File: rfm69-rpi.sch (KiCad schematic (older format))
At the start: 21 parts, among them IC1 RFM69, IC2 RFM69, IC3 RFM69, IC4 RFM69, IC5 NCP1117, IC6 74HC139, J1 RPi_GPIO, P1 COAX, P2 COAX, P3 COAX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

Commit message: Converted to Kicad 5 format; changed direction of INT1
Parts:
- C1, C2: symbol CP -> rfm69-rpi-rescue:CP
- IC1, IC2, IC3, IC4: symbol RFM69 -> rfm69-rpi-rescue:RFM69
- IC5: symbol LD1117S33TR -> rfm69-rpi-rescue:LD1117S33TR
- IC6: symbol 74HC139 -> rfm69-rpi-rescue:74HC139
- J1: symbol RPi_GPIO -> rfm69-rpi-rescue:RPi_GPIO
- JP1, JP2: symbol JUMPER -> rfm69-rpi-rescue:JUMPER
- P1, P2, P3, P4: symbol COAX -> rfm69-rpi-rescue:COAX
- P5: symbol CONN_01X02 -> rfm69-rpi-rescue:CONN_01X02
- R1: symbol R -> rfm69-rpi-rescue:R
- TP1, TP2: symbol TESTPAD -> rfm69-rpi-rescue:TESTPAD
- U1, U2: symbol DS18B20 -> rfm69-rpi-rescue:DS18B20

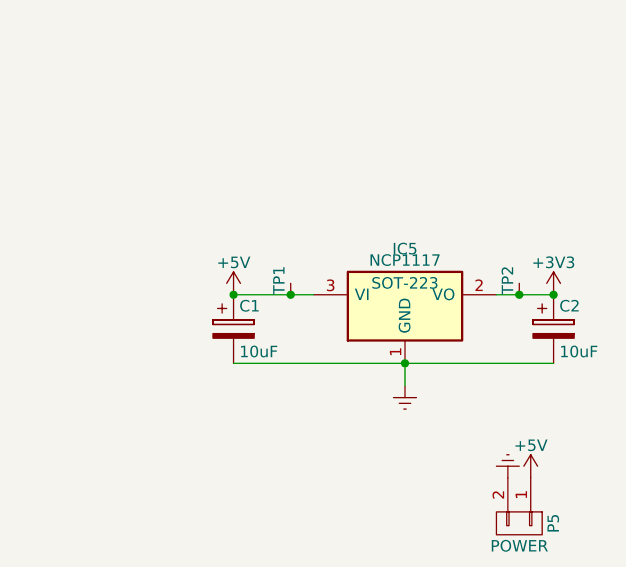
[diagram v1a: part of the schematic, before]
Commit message: Fixed RPi footprint
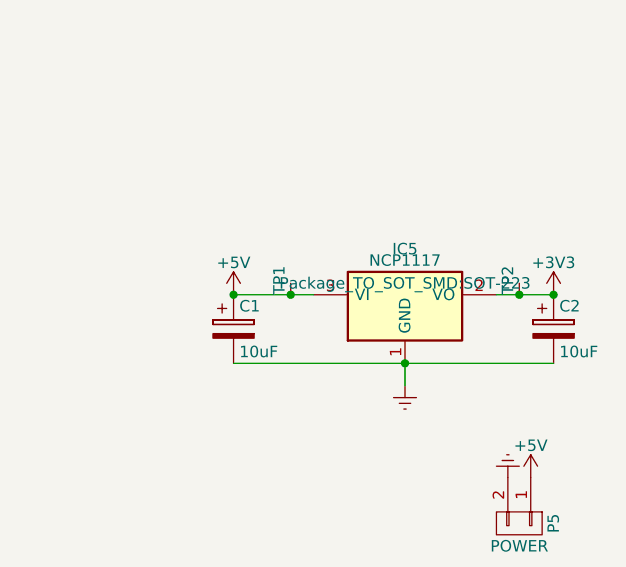
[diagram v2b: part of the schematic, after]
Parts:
- IC5: footprint SOT-223 -> Package_TO_SOT_SMD:SOT-223
- J1: footprint tinkerforge:raspberrypi2 -> pcb-rfm-raspi:raspberrypi2
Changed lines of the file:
@@
 F 0 "IC5" H 9950 5400 50  0000 C CNN
 F 1 "NCP1117" H 9950 5350 50  0000 C CNN
-F 2 "SOT-223" H 9950 5250 50  0000 C CNN
+F 2 "Package_TO_SOT_SMD:SOT-223" H 9950 5250 50  0000 C CNN
 F 3 "" H 9950 5150 50  0000 C CNN
 	1    9950 5150
@@
 F 0 "J1" H 5450 1600 60  0000 C CNN
 F 1 "RPi_GPIO" H 5450 1500 60  0000 C CNN
-F 2 "tinkerforge:raspberrypi2" H 4700 1350 60  0001 C CNN
+F 2 "pcb-rfm-raspi:raspberrypi2" H 4700 1350 60  0001 C CNN
 F 3 "" H 4700 1350 60  0000 C CNN
 	1    4700 1350
